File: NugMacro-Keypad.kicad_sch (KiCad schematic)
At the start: 16 parts, among them J2 Conn_01x04, SW1 SW_Push, U1 ATmega32U4-A, Y1 16MHz

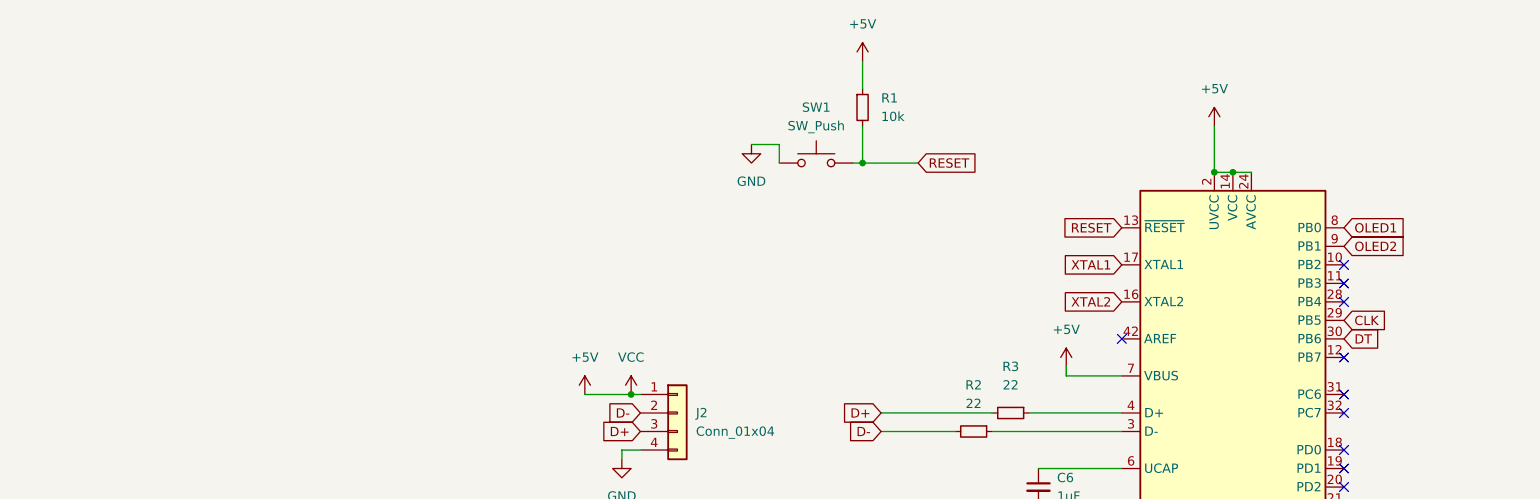
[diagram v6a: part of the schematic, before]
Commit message: Second Version of Rev3 ig?
fixed wiring on oled, made 1.5u key look a bit better, pulled back the jst connector to hopefully make  compatible for a rubber o ring gasket mount.
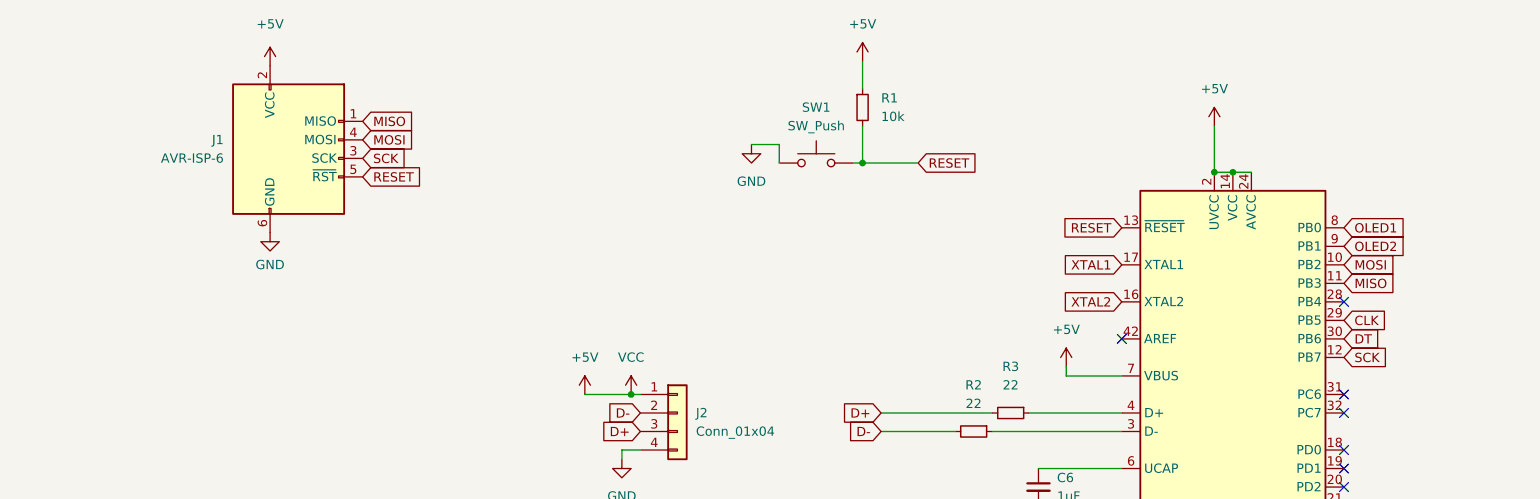
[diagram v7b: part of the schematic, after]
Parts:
- added J1: AVR-ISP-6, random-keyboard-parts:Reset_Pretty-Mask, symbol Connector:AVR-ISP-6
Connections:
- net +5V: now also J1.2 (VCC)
- net GND: now also J1.6 (GND)
- net RESET: now also J1.5 (~{RST})
- net MOSI: now reaches U1.10 (PB2)
- net MOSI: now also J1.4 (MOSI)
- net MISO: now reaches U1.11 (PB3)
- net MISO: now also J1.1 (MISO)
- net SCK: now reaches U1.12 (PB7)
- net SCK: now also J1.3 (SCK)
- no-connect marks 14 -> 11
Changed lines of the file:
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@@
   )
   (no_connect (at 195.58 71.12))
-  (no_connect (at 226.06 73.66))
   (no_connect (at 226.06 88.9))
   (no_connect (at 226.06 86.36))
+  (no_connect (at 226.06 111.76))
   (no_connect (at 226.06 96.52))
   (no_connect (at 226.06 81.28))
-  (no_connect (at 226.06 111.76))
-  (no_connect (at 226.06 60.96))
   (no_connect (at 226.06 93.98))
-  (no_connect (at 226.06 63.5))
   (no_connect (at 226.06 91.44))
   (no_connect (at 226.06 99.06))
@@
     )
   )
+  (global_label "MOSI" (shape input) (at 226.06 60.96 0) (fields_autoplaced)
+    (effects (font (size 1.27 1.27)) (justify left))
+    (property "Intersheet References" "${INTERSHEET_REFS}" (id 0) (at 233.0693 60.8806 0)
+      (effects (font (size 1.27 1.27)) (justify left) hide)
+    )
+  )
+  (global_label "MOSI" (shape input) (at 91.44 43.815 0) (fields_autoplaced)
+    (effects (font (size 1.27 1.27)) (justify left))
+    (property "Intersheet References" "${INTERSHEET_REFS}" (id 0) (at 98.4493 43.7356 0)
+      (effects (font (size 1.27 1.27)) (justify left) hide)
+    )
+  )
   (global_label "ROW0" (shape input) (at 226.06 124.46 0) (fields_autoplaced)
     (effects (font (size 1.27 1.27)) (justify left))
@@
     )
   )
+  (global_label "SCK" (shape input) (at 226.06 73.66 0) (fields_autoplaced)
+    (effects (font (size 1.27 1.27)) (justify left))
+    (property "Intersheet References" "${INTERSHEET_REFS}" (id 0) (at 232.2226 73.5806 0)
+      (effects (font (size 1.27 1.27)) (justify left) hide)
+    )
+  )
   (global_label "XTAL2" (shape input) (at 114.3 105.41 0) (fields_autoplaced)
     (effects (font (size 1.27 1.27)) (justify left))
@@
     )
   )
+  (global_label "SCK" (shape input) (at 91.44 46.355 0) (fields_autoplaced)
+    (effects (font (size 1.27 1.27)) (justify left))
+    (property "Intersheet References" "${INTERSHEET_REFS}" (id 0) (at 97.6026 46.2756 0)
+      (effects (font (size 1.27 1.27)) (justify left) hide)
+    )
+  )
   (global_label "ROW1" (shape input) (at 226.06 121.92 0) (fields_autoplaced)
     (effects (font (size 1.27 1.27)) (justify left))
@@
     )
   )
+  (global_label "RESET" (shape input) (at 91.44 48.895 0) (fields_autoplaced)
+    (effects (font (size 1.27 1.27)) (justify left))
+    (property "Intersheet References" "${INTERSHEET_REFS}" (id 0) (at 99.5983 48.8156 0)
+      (effects (font (size 1.27 1.27)) (justify left) hide)
+    )
+  )
   (global_label "CLK" (shape input) (at 226.06 68.58 0) (fields_autoplaced)
     (effects (font (size 1.27 1.27)) (justify left))
@@
     )
   )
+  (global_label "MISO" (shape input) (at 91.44 41.275 0) (fields_autoplaced)
+    (effects (font (size 1.27 1.27)) (justify left))
+    (property "Intersheet References" "${INTERSHEET_REFS}" (id 0) (at 98.4493 41.1956 0)
+      (effects (font (size 1.27 1.27)) (justify left) hide)
+    )
+  )
   (global_label "RESET" (shape input) (at 167.64 46.99 0) (fields_autoplaced)
     (effects (font (size 1.27 1.27)) (justify left))
     (property "Intersheet References" "${INTERSHEET_REFS}" (id 0) (at 175.7983 46.9106 0)
+      (effects (font (size 1.27 1.27)) (justify left) hide)
+    )
+  )
+  (global_label "MISO" (shape input) (at 226.06 63.5 0) (fields_autoplaced)
+    (effects (font (size 1.27 1.27)) (justify left))
+    (property "Intersheet References" "${INTERSHEET_REFS}" (id 0) (at 233.0693 63.4206 0)
       (effects (font (size 1.27 1.27)) (justify left) hide)
     )
@@
     (pin "1")
   )
+  (symbol (lib_id "power:GND") (at 78.74 56.515 0) (unit 1)
+    (in_bom yes) (on_board yes) (fields_autoplaced)
+    (property "Reference" "#PWR0102" (id 0) (at 78.74 62.865 0)
+      (effects (font (size 1.27 1.27)) hide)
+    )
+    (property "Value" "GND" (id 1) (at 78.74 60.96 0))
+    (property "Footprint" "" (id 2) (at 78.74 56.515 0)
+      (effects (font (size 1.27 1.27)) hide)
+    )
+    (property "Datasheet" "" (id 3) (at 78.74 56.515 0)
+      (effects (font (size 1.27 1.27)) hide)
+    )
+    (pin "1")
+  )
   (symbol (lib_id "power:GND") (at 144.78 44.45 0) (unit 1)
     (in_bom yes) (on_board yes) (fields_autoplaced)
@@
     (pin "1")
     (pin "2")
+  )
+  (symbol (lib_id "Connector:AVR-ISP-6") (at 81.28 46.355 0) (unit 1)
+    (in_bom yes) (on_board yes) (fields_autoplaced)
+    (property "Reference" "J1" (id 0) (at 72.39 43.8149 0)
+      (effects (font (size 1.27 1.27)) (justify right))
+    )
+    (property "Value" "AVR-ISP-6" (id 1) (at 72.39 46.3549 0)
+      (effects (font (size 1.27 1.27)) (justify right))
+    )
+    (property "Footprint" "random-keyboard-parts:Reset_Pretty-Mask" (id 2) (at 74.93 45.085 90)
+      (effects (font (size 1.27 1.27)) hide)
+    )
+    (property "Datasheet" " ~" (id 3) (at 48.895 60.325 0)
+      (effects (font (size 1.27 1.27)) hide)
+    )
+    (pin "1")
+    (pin "2")
+    (pin "3")
+    (pin "4")
+    (pin "5")
+    (pin "6")
   )
   (symbol (lib_id "Device:C_Small") (at 91.44 107.95 270) (unit 1)
@@
     (pin "1")
   )
+  (symbol (lib_id "power:+5V") (at 78.74 33.655 0) (unit 1)
+    (in_bom yes) (on_board yes) (fields_autoplaced)
+    (property "Reference" "#PWR0101" (id 0) (at 78.74 37.465 0)
+      (effects (font (size 1.27 1.27)) hide)
+    )
+    (property "Value" "+5V" (id 1) (at 78.74 27.94 0))
+    (property "Footprint" "" (id 2) (at 78.74 33.655 0)
+      (effects (font (size 1.27 1.27)) hide)
+    )
+    (property "Datasheet" "" (id 3) (at 78.74 33.655 0)
+      (effects (font (size 1.27 1.27)) hide)
+    )
+    (pin "1")
+  )
   (sheet (at 31.75 137.16) (size 88.9 54.61) (fields_autoplaced)
     (stroke (width 0.1524) (type solid) (color 0 0 0 0))
@@
   )
   (symbol_instances
+    (path "/fab98c12-bdc0-44d2-89ae-178851337d62"
+      (reference "#PWR0101") (unit 1) (value "+5V") (footprint "")
+    )
+    (path "/55cbcbc6-1393-4d01-bb82-9b3794a6e130"
+      (reference "#PWR0102") (unit 1) (value "GND") (footprint "")
+    )
     (path "/f6c50297-e7e3-4156-8463-966e3492b299"
       (reference "#PWR0103") (unit 1) (value "+5V") (footprint "")
@@
       (reference "D16") (unit 1) (value "D_Small") (footprint "Diode_SMD:D_SOD-123")
     )
+    (path "/6bfb3e63-3957-449c-8e31-f4cae22a544e"
+      (reference "J1") (unit 1) (value "AVR-ISP-6") (footprint "random-keyboard-parts:Reset_Pretty-Mask")
+    )
     (path "/000c8317-96e0-4563-8e9d-728bb31873d2"

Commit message: just double checked some possible design rule issues
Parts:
- removed J1: AVR-ISP-6, random-keyboard-parts:Reset_Pretty-Mask, symbol Connector:AVR-ISP-6
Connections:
- net OLED1: now also U1.9 (PB1); no longer U1.8 (PB0)
- net OLED2: now also U1.8 (PB0); no longer U1.9 (PB1)
- net MISO: no longer names the net of U1.11 (PB3)
- net MOSI: no longer names the net of U1.10 (PB2)
- net SCK: no longer names the net of U1.12 (PB7)
- no-connect marks 11 -> 14
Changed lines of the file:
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@@
   (no_connect (at 226.06 86.36))
   (no_connect (at 226.06 111.76))
+  (no_connect (at 226.06 60.96))
   (no_connect (at 226.06 96.52))
   (no_connect (at 226.06 81.28))
+  (no_connect (at 226.06 73.66))
   (no_connect (at 226.06 93.98))
   (no_connect (at 226.06 91.44))
   (no_connect (at 226.06 99.06))
   (no_connect (at 226.06 66.04))
+  (no_connect (at 226.06 63.5))
   (no_connect (at 226.06 78.74))
   (wire (pts (xy 195.58 76.2) (xy 187.96 76.2))
@@
     )
   )
-  (global_label "MOSI" (shape input) (at 226.06 60.96 0) (fields_autoplaced)
-    (effects (font (size 1.27 1.27)) (justify left))
-    (property "Intersheet References" "${INTERSHEET_REFS}" (id 0) (at 233.0693 60.8806 0)
-      (effects (font (size 1.27 1.27)) (justify left) hide)
-    )
-  )
-  (global_label "MOSI" (shape input) (at 91.44 43.815 0) (fields_autoplaced)
-    (effects (font (size 1.27 1.27)) (justify left))
-    (property "Intersheet References" "${INTERSHEET_REFS}" (id 0) (at 98.4493 43.7356 0)
-      (effects (font (size 1.27 1.27)) (justify left) hide)
-    )
-  )
   (global_label "ROW0" (shape input) (at 226.06 124.46 0) (fields_autoplaced)
     (effects (font (size 1.27 1.27)) (justify left))
@@
     )
   )
-  (global_label "SCK" (shape input) (at 226.06 73.66 0) (fields_autoplaced)
-    (effects (font (size 1.27 1.27)) (justify left))
-    (property "Intersheet References" "${INTERSHEET_REFS}" (id 0) (at 232.2226 73.5806 0)
-      (effects (font (size 1.27 1.27)) (justify left) hide)
-    )
-  )
   (global_label "XTAL2" (shape input) (at 114.3 105.41 0) (fields_autoplaced)
     (effects (font (size 1.27 1.27)) (justify left))
@@
     )
   )
-  (global_label "OLED2" (shape input) (at 226.06 58.42 0) (fields_autoplaced)
-    (effects (font (size 1.27 1.27)) (justify left))
-    (property "Intersheet References" "${INTERSHEET_REFS}" (id 0) (at 234.4602 58.3406 0)
+  (global_label "OLED2" (shape input) (at 226.06 55.88 0) (fields_autoplaced)
+    (effects (font (size 1.27 1.27)) (justify left))
+    (property "Intersheet References" "${INTERSHEET_REFS}" (id 0) (at 234.4602 55.8006 0)
       (effects (font (size 1.27 1.27)) (justify left) hide)
     )
@@
     (effects (font (size 1.27 1.27)) (justify left))
     (property "Intersheet References" "${INTERSHEET_REFS}" (id 0) (at 123.4864 100.2506 0)
-      (effects (font (size 1.27 1.27)) (justify left) hide)
-    )
-  )
-  (global_label "SCK" (shape input) (at 91.44 46.355 0) (fields_autoplaced)
-    (effects (font (size 1.27 1.27)) (justify left))
-    (property "Intersheet References" "${INTERSHEET_REFS}" (id 0) (at 97.6026 46.2756 0)
       (effects (font (size 1.27 1.27)) (justify left) hide)
     )
@@
     )
   )
-  (global_label "RESET" (shape input) (at 91.44 48.895 0) (fields_autoplaced)
-    (effects (font (size 1.27 1.27)) (justify left))
-    (property "Intersheet References" "${INTERSHEET_REFS}" (id 0) (at 99.5983 48.8156 0)
-      (effects (font (size 1.27 1.27)) (justify left) hide)
-    )
-  )
   (global_label "CLK" (shape input) (at 226.06 68.58 0) (fields_autoplaced)
     (effects (font (size 1.27 1.27)) (justify left))
@@
     )
   )
-  (global_label "MISO" (shape input) (at 91.44 41.275 0) (fields_autoplaced)
-    (effects (font (size 1.27 1.27)) (justify left))
-    (property "Intersheet References" "${INTERSHEET_REFS}" (id 0) (at 98.4493 41.1956 0)
-      (effects (font (size 1.27 1.27)) (justify left) hide)
-    )
-  )
   (global_label "RESET" (shape input) (at 167.64 46.99 0) (fields_autoplaced)
     (effects (font (size 1.27 1.27)) (justify left))
     (property "Intersheet References" "${INTERSHEET_REFS}" (id 0) (at 175.7983 46.9106 0)
-      (effects (font (size 1.27 1.27)) (justify left) hide)
-    )
-  )
-  (global_label "MISO" (shape input) (at 226.06 63.5 0) (fields_autoplaced)
-    (effects (font (size 1.27 1.27)) (justify left))
-    (property "Intersheet References" "${INTERSHEET_REFS}" (id 0) (at 233.0693 63.4206 0)
       (effects (font (size 1.27 1.27)) (justify left) hide)
     )
@@
     )
   )
-  (global_label "OLED1" (shape input) (at 226.06 55.88 0) (fields_autoplaced)
-    (effects (font (size 1.27 1.27)) (justify left))
-    (property "Intersheet References" "${INTERSHEET_REFS}" (id 0) (at 234.4602 55.8006 0)
+  (global_label "OLED1" (shape input) (at 226.06 58.42 0) (fields_autoplaced)
+    (effects (font (size 1.27 1.27)) (justify left))
+    (property "Intersheet References" "${INTERSHEET_REFS}" (id 0) (at 234.4602 58.3406 0)
       (effects (font (size 1.27 1.27)) (justify left) hide)
     )
@@
     (pin "1")
   )
-  (symbol (lib_id "power:GND") (at 78.74 56.515 0) (unit 1)
-    (in_bom yes) (on_board yes) (fields_autoplaced)
-    (property "Reference" "#PWR0102" (id 0) (at 78.74 62.865 0)
-      (effects (font (size 1.27 1.27)) hide)
-    )
-    (property "Value" "GND" (id 1) (at 78.74 60.96 0))
-    (property "Footprint" "" (id 2) (at 78.74 56.515 0)
-      (effects (font (size 1.27 1.27)) hide)
-    )
-    (property "Datasheet" "" (id 3) (at 78.74 56.515 0)
-      (effects (font (size 1.27 1.27)) hide)
-    )
-    (pin "1")
-  )
   (symbol (lib_id "power:GND") (at 144.78 44.45 0) (unit 1)
     (in_bom yes) (on_board yes) (fields_autoplaced)
@@
     (pin "1")
     (pin "2")
-  )
-  (symbol (lib_id "Connector:AVR-ISP-6") (at 81.28 46.355 0) (unit 1)
-    (in_bom yes) (on_board yes) (fields_autoplaced)
-    (property "Reference" "J1" (id 0) (at 72.39 43.8149 0)
-      (effects (font (size 1.27 1.27)) (justify right))
-    )
-    (property "Value" "AVR-ISP-6" (id 1) (at 72.39 46.3549 0)
-      (effects (font (size 1.27 1.27)) (justify right))
-    )
-    (property "Footprint" "random-keyboard-parts:Reset_Pretty-Mask" (id 2) (at 74.93 45.085 90)
-      (effects (font (size 1.27 1.27)) hide)
-    )
-    (property "Datasheet" " ~" (id 3) (at 48.895 60.325 0)
-      (effects (font (size 1.27 1.27)) hide)
-    )
-    (pin "1")
-    (pin "2")
-    (pin "3")
-    (pin "4")
-    (pin "5")
-    (pin "6")
   )
   (symbol (lib_id "Device:C_Small") (at 91.44 107.95 270) (unit 1)
@@
     (pin "1")
   )
-  (symbol (lib_id "power:+5V") (at 78.74 33.655 0) (unit 1)
-    (in_bom yes) (on_board yes) (fields_autoplaced)
-    (property "Reference" "#PWR0101" (id 0) (at 78.74 37.465 0)
-      (effects (font (size 1.27 1.27)) hide)
-    )
-    (property "Value" "+5V" (id 1) (at 78.74 27.94 0))
-    (property "Footprint" "" (id 2) (at 78.74 33.655 0)
-      (effects (font (size 1.27 1.27)) hide)
-    )
-    (property "Datasheet" "" (id 3) (at 78.74 33.655 0)
-      (effects (font (size 1.27 1.27)) hide)
-    )
-    (pin "1")
-  )
   (sheet (at 31.75 137.16) (size 88.9 54.61) (fields_autoplaced)
     (stroke (width 0.1524) (type solid) (color 0 0 0 0))
@@
   )
   (symbol_instances
-    (path "/fab98c12-bdc0-44d2-89ae-178851337d62"
-      (reference "#PWR0101") (unit 1) (value "+5V") (footprint "")
-    )
-    (path "/55cbcbc6-1393-4d01-bb82-9b3794a6e130"
-      (reference "#PWR0102") (unit 1) (value "GND") (footprint "")
-    )
     (path "/f6c50297-e7e3-4156-8463-966e3492b299"
       (reference "#PWR0103") (unit 1) (value "+5V") (footprint "")
@@
       (reference "D16") (unit 1) (value "D_Small") (footprint "Diode_SMD:D_SOD-123")
     )
-    (path "/6bfb3e63-3957-449c-8e31-f4cae22a544e"
-      (reference "J1") (unit 1) (value "AVR-ISP-6") (footprint "random-keyboard-parts:Reset_Pretty-Mask")
-    )
     (path "/000c8317-96e0-4563-8e9d-728bb31873d2"
